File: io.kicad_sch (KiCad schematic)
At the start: 5 parts, among them U16 W65C22SxP

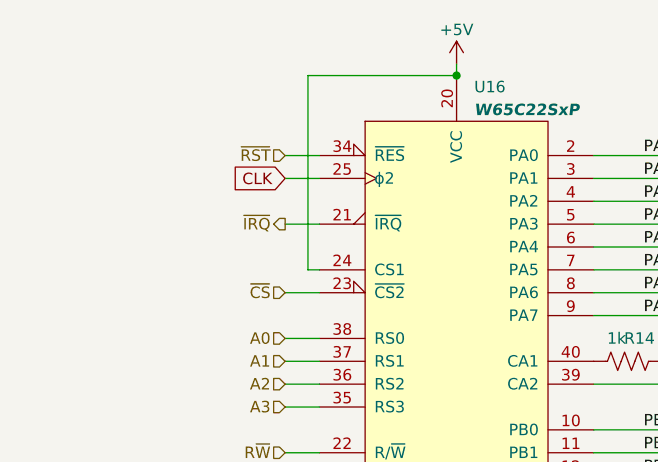
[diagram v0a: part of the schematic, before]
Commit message: RS-232/ACIA works!
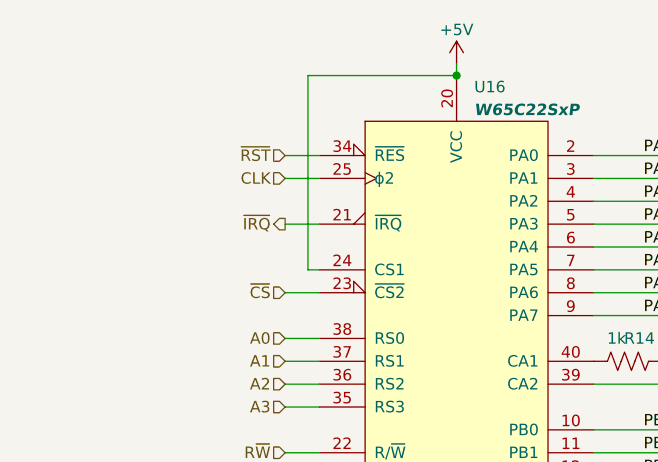
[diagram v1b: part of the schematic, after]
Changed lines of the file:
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@@
     (effects (font (size 1.27 1.27)) (justify right bottom))
-  )
-  (global_label "CLK" (shape input) (at 44.45 35.56 180) (fields_autoplaced)
-    (effects (font (size 1.27 1.27)) (justify right))
-    (property "Intersheetrefs" "${INTERSHEET_REFS}" (at 37.9761 35.56 0)
-      (effects (font (size 1.27 1.27)) (justify right) hide)
-    )
   )
   (hierarchical_label "R~{W}" (shape input) (at 44.45 66.04 180) (fields_autoplaced)
@@
     (effects (font (size 1.27 1.27)) (justify left))
   )
+  (hierarchical_label "CLK" (shape input) (at 44.45 35.56 180) (fields_autoplaced)
+    (effects (font (size 1.27 1.27)) (justify right))
+  )
   (hierarchical_label "~{IRQ}" (shape output) (at 44.45 40.64 180) (fields_autoplaced)
